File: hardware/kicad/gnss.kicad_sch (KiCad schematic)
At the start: 0 parts

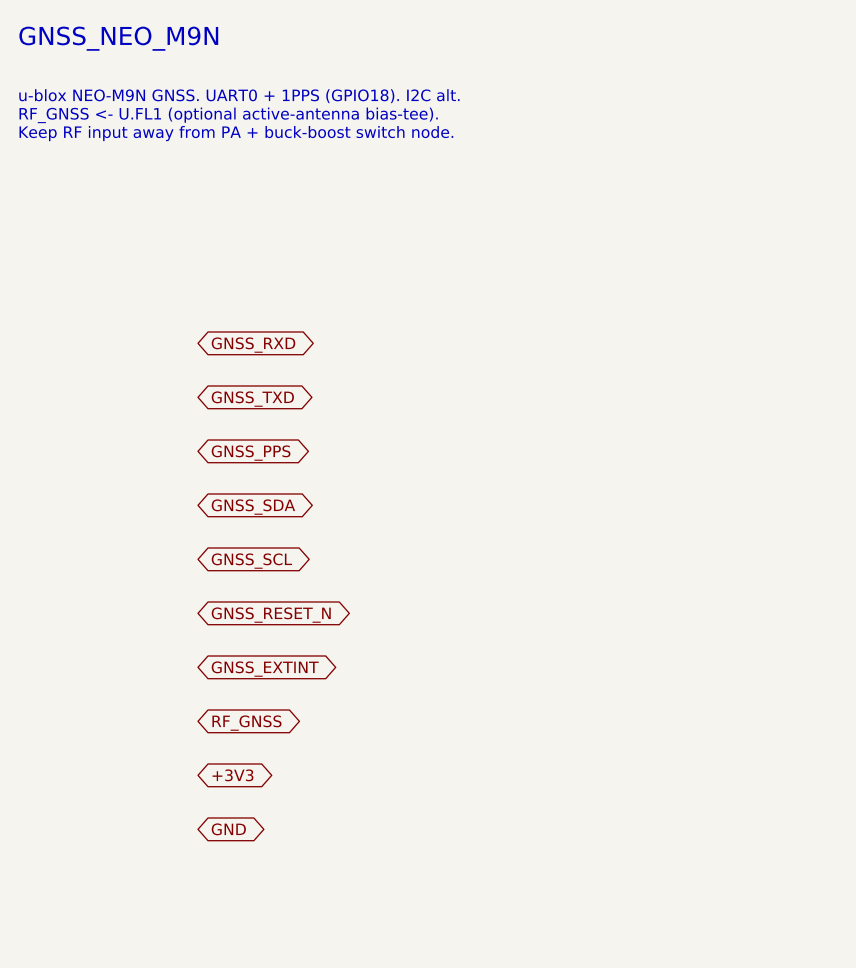
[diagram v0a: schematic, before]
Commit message: Deepen design to component level + fix EEPROM power rail
- Fix: HAT ID EEPROM (U6) now powered from Pi header 3V3 (3V3_PI, pin 1)
  so it is readable at boot before the HAT's own 3V3 comes up (was
  incorrectly on the HAT 3V3 regulator).
- Add docs/SCHEMATIC.md: component-level subcircuits for every block
  (refdes + values + nets) — buck-boost/3V3 FB dividers, MM8108 SPI
  termination/pulls, E21 RF DC-blocks/attenuator pad/T-R pulldowns,
  NEO-M9N active-antenna bias via VCC_RF, ID EEPROM (WP default).
- Add docs/BRINGUP.md: stage-gated power-on + RF test plan (don't key
  the 1W PA until rails/drive-level/FEM-timing verified).
- Add GNSS VCC_RF antenna bias + +3V3_GNSS ferrite to the net list.
- Enrich KiCad sub-sheets with per-block refdes notes and the new nets;
  regenerate scaffold (KiCad 10 format, S-expression balance re-checked).
- BOM: concrete passives (RF DC-blocks, attenuator pad, ferrite, TVS,
  FB dividers, WP jumper).

https://claude.ai/code/session_015nkkW85U3sPf5mcvrsMw7T
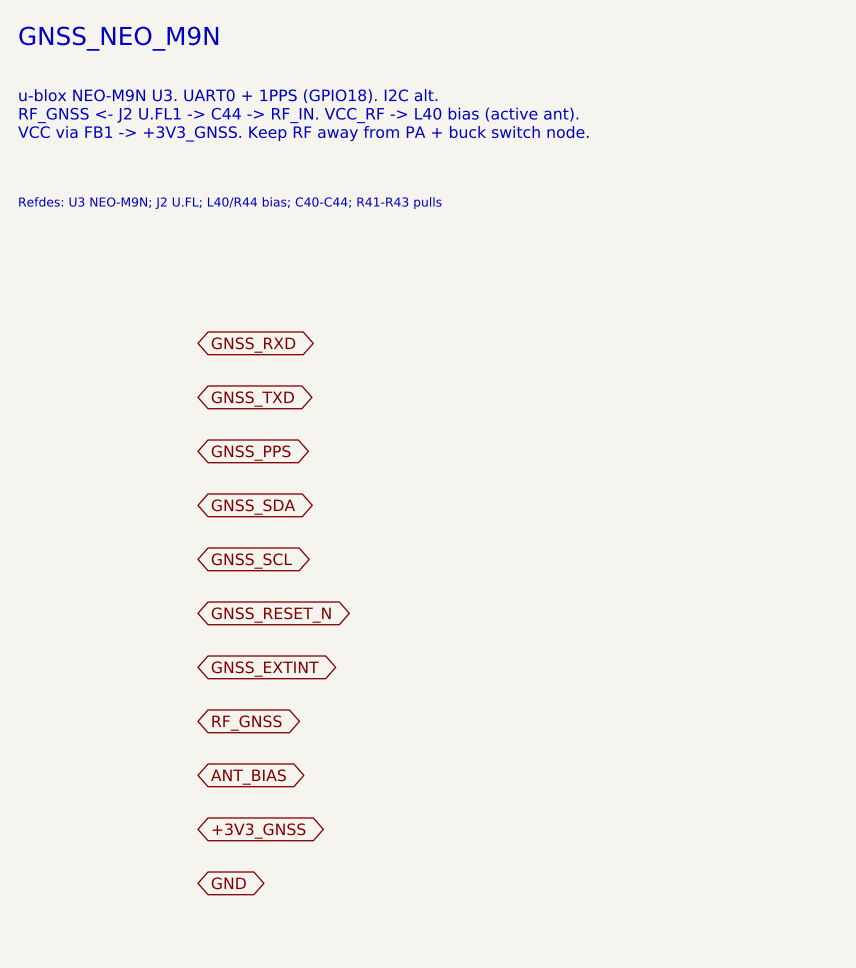
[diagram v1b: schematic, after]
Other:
- note added: "Refdes: U3 NEO-M9N; J2 U.FL; L40/R44 bias; C40-C44; R41-R43 pulls"
- note added: "u-blox NEO-M9N U3. UART0 + 1PPS (GPIO18). I2C alt. RF_GNSS <- J2 U.FL1 -> C44 -> RF_IN. VCC_RF -> L40 bias (active ant). VCC via FB1 -> +3V3_GNSS. Keep RF away from PA + buck switch node."
- note removed: "u-blox NEO-M9N GNSS. UART0 + 1PPS (GPIO18). I2C alt. RF_GNSS <- U.FL1 (optional active-antenna bias-tee). Keep RF input away from PA + buck-boost switch node."
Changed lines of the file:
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@@
 	(paper "A4")
 	(text "GNSS_NEO_M9N" (exclude_from_sim no) (at 20 15 0) (effects (font (size 2 2) (thickness 0.3)) (justify left top)))
-	(text "u-blox NEO-M9N GNSS. UART0 + 1PPS (GPIO18). I2C alt.\nRF_GNSS <- U.FL1 (optional active-antenna bias-tee).\nKeep RF input away from PA + buck-boost switch node." (exclude_from_sim no) (at 20 22 0) (effects (font (size 1.27 1.27)) (justify left top)))
+	(text "u-blox NEO-M9N U3. UART0 + 1PPS (GPIO18). I2C alt.\nRF_GNSS <- J2 U.FL1 -> C44 -> RF_IN. VCC_RF -> L40 bias (active ant).\nVCC via FB1 -> +3V3_GNSS. Keep RF away from PA + buck switch node." (exclude_from_sim no) (at 20 22 0) (effects (font (size 1.27 1.27)) (justify left top)))
+	(text "Refdes: U3 NEO-M9N; J2 U.FL; L40/R44 bias; C40-C44; R41-R43 pulls" (exclude_from_sim no) (at 20 34 0) (effects (font (size 1.0 1.0)) (justify left top)))
 	(global_label "GNSS_RXD" (shape bidirectional) (at 40 50 0) (fields_autoplaced yes) (effects (font (size 1.27 1.27)) (justify left)))
 	(global_label "GNSS_TXD" (shape bidirectional) (at 40 56 0) (fields_autoplaced yes) (effects (font (size 1.27 1.27)) (justify left)))
@@
 	(global_label "GNSS_EXTINT" (shape bidirectional) (at 40 86 0) (fields_autoplaced yes) (effects (font (size 1.27 1.27)) (justify left)))
 	(global_label "RF_GNSS" (shape bidirectional) (at 40 92 0) (fields_autoplaced yes) (effects (font (size 1.27 1.27)) (justify left)))
-	(global_label "+3V3" (shape bidirectional) (at 40 98 0) (fields_autoplaced yes) (effects (font (size 1.27 1.27)) (justify left)))
-	(global_label "GND" (shape bidirectional) (at 40 104 0) (fields_autoplaced yes) (effects (font (size 1.27 1.27)) (justify left)))
+	(global_label "ANT_BIAS" (shape bidirectional) (at 40 98 0) (fields_autoplaced yes) (effects (font (size 1.27 1.27)) (justify left)))
+	(global_label "+3V3_GNSS" (shape bidirectional) (at 40 104 0) (fields_autoplaced yes) (effects (font (size 1.27 1.27)) (justify left)))
+	(global_label "GND" (shape bidirectional) (at 40 110 0) (fields_autoplaced yes) (effects (font (size 1.27 1.27)) (justify left)))
 )

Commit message: Add gap-analysis components (datasheet-grounded) + RTC
Read the uploaded datasheets (MM8108-MF15457, E21-900G30S, NEO-M9N-00B)
and resolved the component gaps:

- #1/#2 RESOLVED by the module: MF15457 is self-contained (internal
  clock+PMU+PA); only needs VBAT/VBAT_TX/VDDIO 3.0-3.6 V. No external SoC
  inductors, 1V8/1V2 rails, or TCXO.
- VPA fixed at 5.0 V (E21 needs 4.75-5.25 V, ~620 mA TX, +20 dBm in ->
  +30 dBm out, 12 dB gain). Real pinouts wired (module 38-pin; E21
  pin6=PIN xcvr, pin9=ANT).
- Architecture finding: module has integrated PA + single ANT pin and NO
  hardware T/R FEM line. External E21 now needs (a) ~3-5 dB drive pad,
  (b) T/R control via module GPIO0/1 toggled by OpenMANET FW (or RF-sense
  auto-T/R fallback), and (c) end-product recertification at +30 dBm.

Added components:
- N3 900 MHz harmonic LPF (FL2); N4 inrush soft-start load switch (U10);
  N5 supervisor (U11); N6 radio-rail load switch (U12, OpenMANET
  power-gpios); N7 RF shields; N8 GNSS antenna ESD (D8); N9 status LEDs;
  N10 E21 thermal relief.
- RTC: RV-3028-C7 (U13) on I2C1 0x52 with a soldered rechargeable cell
  (BT1, trickle-charged) per request; added to the device-tree overlay.
- Declined per request: debug UART/JTAG pads, test points.

Updated docs (new COMPONENTS_GAP.md; DECISIONS B1-B9; SCHEMATIC; BOM;
POWER budget), netlist, overlay, and regenerated the KiCad 10 scaffold
with the new nets. Committed the vendor datasheets under hardware/.

https://claude.ai/code/session_015nkkW85U3sPf5mcvrsMw7T
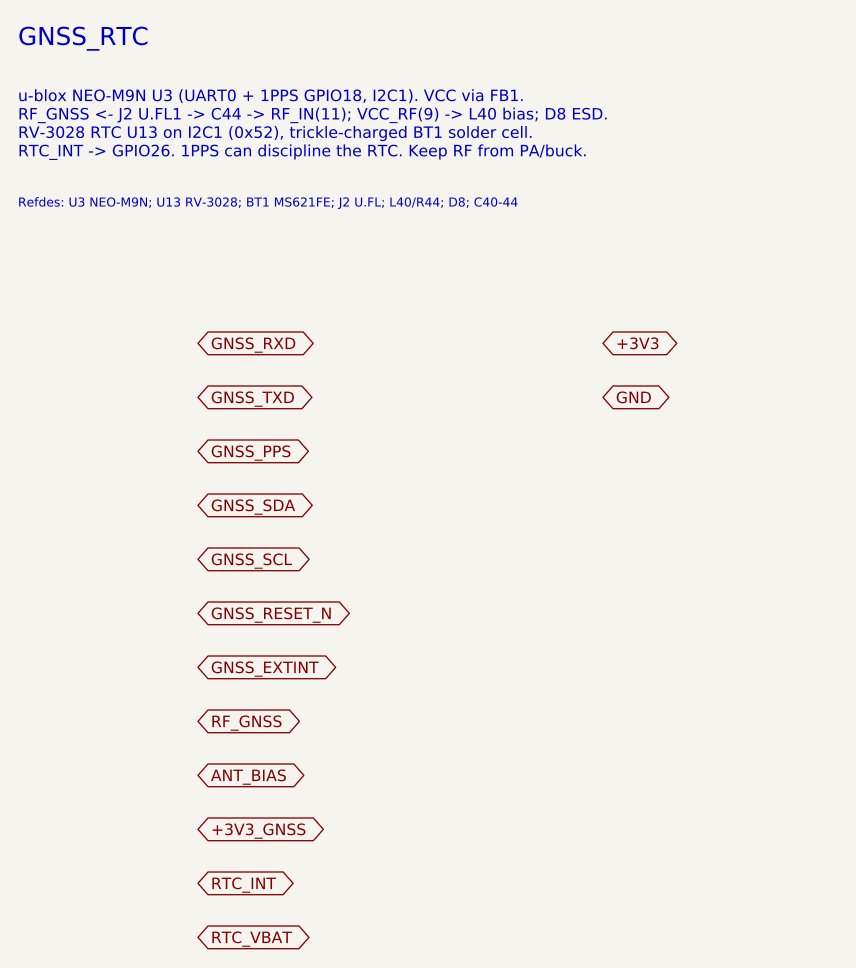
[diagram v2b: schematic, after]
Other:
- note added: "GNSS_RTC"
- note added: "Refdes: U3 NEO-M9N; U13 RV-3028; BT1 MS621FE; J2 U.FL; L40/R44; D8; C40-44"
- note added: "u-blox NEO-M9N U3 (UART0 + 1PPS GPIO18, I2C1). VCC via FB1. RF_GNSS <- J2 U.FL1 -> C44 -> RF_IN(11); VCC_RF(9) -> L40 bias; D8 ESD. RV-3028 RTC U13 on I2C1 (0x52), trickle-charged BT1 solder cell. RTC_INT -> GPIO26. 1PPS can discipline the RTC. Keep RF from PA/buck."
- note removed: "GNSS_NEO_M9N"
- note removed: "Refdes: U3 NEO-M9N; J2 U.FL; L40/R44 bias; C40-C44; R41-R43 pulls"
- note removed: "u-blox NEO-M9N U3. UART0 + 1PPS (GPIO18). I2C alt. RF_GNSS <- J2 U.FL1 -> C44 -> RF_IN. VCC_RF -> L40 bias (active ant). VCC via FB1 -> +3V3_GNSS. Keep RF away from PA + buck switch node."
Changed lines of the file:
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@@
 	(generator_version "10.0")
 	(paper "A4")
-	(text "GNSS_NEO_M9N" (exclude_from_sim no) (at 20 15 0) (effects (font (size 2 2) (thickness 0.3)) (justify left top)))
-	(text "u-blox NEO-M9N U3. UART0 + 1PPS (GPIO18). I2C alt.\nRF_GNSS <- J2 U.FL1 -> C44 -> RF_IN. VCC_RF -> L40 bias (active ant).\nVCC via FB1 -> +3V3_GNSS. Keep RF away from PA + buck switch node." (exclude_from_sim no) (at 20 22 0) (effects (font (size 1.27 1.27)) (justify left top)))
-	(text "Refdes: U3 NEO-M9N; J2 U.FL; L40/R44 bias; C40-C44; R41-R43 pulls" (exclude_from_sim no) (at 20 34 0) (effects (font (size 1.0 1.0)) (justify left top)))
+	(text "GNSS_RTC" (exclude_from_sim no) (at 20 15 0) (effects (font (size 2 2) (thickness 0.3)) (justify left top)))
+	(text "u-blox NEO-M9N U3 (UART0 + 1PPS GPIO18, I2C1). VCC via FB1.\nRF_GNSS <- J2 U.FL1 -> C44 -> RF_IN(11); VCC_RF(9) -> L40 bias; D8 ESD.\nRV-3028 RTC U13 on I2C1 (0x52), trickle-charged BT1 solder cell.\nRTC_INT -> GPIO26. 1PPS can discipline the RTC. Keep RF from PA/buck." (exclude_from_sim no) (at 20 22 0) (effects (font (size 1.27 1.27)) (justify left top)))
+	(text "Refdes: U3 NEO-M9N; U13 RV-3028; BT1 MS621FE; J2 U.FL; L40/R44; D8; C40-44" (exclude_from_sim no) (at 20 34 0) (effects (font (size 1.0 1.0)) (justify left top)))
 	(global_label "GNSS_RXD" (shape bidirectional) (at 40 50 0) (fields_autoplaced yes) (effects (font (size 1.27 1.27)) (justify left)))
 	(global_label "GNSS_TXD" (shape bidirectional) (at 40 56 0) (fields_autoplaced yes) (effects (font (size 1.27 1.27)) (justify left)))
@@
 	(global_label "ANT_BIAS" (shape bidirectional) (at 40 98 0) (fields_autoplaced yes) (effects (font (size 1.27 1.27)) (justify left)))
 	(global_label "+3V3_GNSS" (shape bidirectional) (at 40 104 0) (fields_autoplaced yes) (effects (font (size 1.27 1.27)) (justify left)))
-	(global_label "GND" (shape bidirectional) (at 40 110 0) (fields_autoplaced yes) (effects (font (size 1.27 1.27)) (justify left)))
+	(global_label "RTC_INT" (shape bidirectional) (at 40 110 0) (fields_autoplaced yes) (effects (font (size 1.27 1.27)) (justify left)))
+	(global_label "RTC_VBAT" (shape bidirectional) (at 40 116 0) (fields_autoplaced yes) (effects (font (size 1.27 1.27)) (justify left)))
+	(global_label "+3V3" (shape bidirectional) (at 85 50 0) (fields_autoplaced yes) (effects (font (size 1.27 1.27)) (justify left)))
+	(global_label "GND" (shape bidirectional) (at 85 56 0) (fields_autoplaced yes) (effects (font (size 1.27 1.27)) (justify left)))
 )
